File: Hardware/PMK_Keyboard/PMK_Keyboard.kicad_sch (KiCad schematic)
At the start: 51 parts, among them IC1 SN74HC165PWR, IC2 SN74HC165PWR, IC3 SN74HC165PWR, IC4 SN74HC165PWR, IC5 SN74HC165PWR, IC7 ESP32-S2FH4, SW1 SW_Push, SW10 SW_Push, SW11 SW_Push, SW12 SW_Push, SW13 SW_Push, SW14 SW_Push, SW15 SW_Push, SW16 SW_Push, SW17 SW_Push, SW18 SW_Push, SW19 SW_Push, SW2 SW_Push, SW20 SW_Push, SW21 SW_Push, SW22 SW_Push, SW23 SW_Push, SW24 SW_Push, SW25 SW_Push, SW26 SW_Push, SW27 SW_Push, SW28 SW_Push, SW29 SW_Push, SW3 SW_Push, SW30 SW_Push, SW31 SW_Push, SW32 SW_Push, SW33 SW_Push, SW34 SW_Push, SW35 SW_Push, SW36 SW_Push, SW37 SW_Push, SW38 SW_Push, SW39 SW_Push, SW4 SW_Push, SW40 SW_Push, SW5 SW_Push, SW6 SW_Push, SW7 SW_Push, SW8 SW_Push, SW9 SW_Push

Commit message: changed switch footprint
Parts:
- SW1, SW10, SW11, SW12, SW13, SW14, SW15, SW16, SW17, SW18, SW19, SW2, SW20, SW21, SW22, SW23, SW24, SW25, SW26, SW27, SW28, SW29, SW3, SW30, SW31, SW32, SW33, SW34, SW35, SW36, SW37, SW38, SW39, SW4, SW5, SW6, SW7, SW8, SW9: footprint Component_lib:Kailh_socket_PG1350_optional_reversible -> Component_lib:Kailh_socket_PG1350_reversible

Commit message: Started routing
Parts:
- SW40: footprint Component_lib:SKRPABE010 -> Component_lib:Kailh_socket_PG1350_reversible
- SW8: footprint Component_lib:Kailh_socket_PG1350_reversible -> Component_lib:SKRPABE010
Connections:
- net 1: now also SW1.1; no longer SW1.2
- net 10: now also SW10.1; no longer SW10.2
- net 11: now also SW11.1; no longer SW11.2
- net 12: now also SW12.1; no longer SW12.2
- net 13: now also SW13.1; no longer SW13.2
- net 14: now also SW14.1; no longer SW14.2
- net 15: now also SW15.1; no longer SW15.2
- net 16: now also SW16.1; no longer SW16.2
- net 17: now also SW17.1; no longer SW17.2
- net 18: now also SW18.1; no longer SW18.2
- net 19: now also SW19.1; no longer SW19.2
- net 2: now also SW2.1; no longer SW2.2
- net 20: now also SW20.1; no longer SW20.2
- net 21: now also SW21.1; no longer SW21.2
- net 22: now also SW22.1; no longer SW22.2
- net 23: now also SW23.1; no longer SW23.2
- net 24: now also SW24.1; no longer SW24.2
- net 25: now also SW25.1; no longer SW25.2
- net 26: now also SW26.1; no longer SW26.2
- net 27: now also SW27.1; no longer SW27.2
- net 28: now also SW28.1; no longer SW28.2
- net 29: now also SW29.1; no longer SW29.2
- net 3: now also SW3.1; no longer SW3.2
- net 30: now also SW30.1; no longer SW30.2
- net 31: now also SW31.1; no longer SW31.2
- net 32: now also SW32.1; no longer SW32.2
- net 33: now also SW33.1; no longer SW33.2
- net 34: now also SW34.1; no longer SW34.2
- net 35: now also SW35.1; no longer SW35.2
- net 36: now also SW36.1; no longer SW36.2
- net 37: now also SW37.1; no longer SW37.2
- net 38: now also SW38.1; no longer SW38.2
- net 39: now also SW39.1; no longer SW39.2
- net 4: now also SW4.1; no longer SW4.2
- net 40: now also SW40.1; no longer SW40.2
- net 5: now also SW5.1; no longer SW5.2
- net 6: now also SW6.1; no longer SW6.2
- net 7: now also SW7.1; no longer SW7.2
- net 8: now also SW8.1; no longer SW8.2
- net 9: now also SW9.1; no longer SW9.2
- net GND: now also SW1.2, SW10.2, SW11.2, SW12.2, SW13.2, SW14.2, SW15.2, SW16.2, SW17.2, SW18.2, SW19.2, SW2.2, SW20.2, SW21.2, SW22.2, SW23.2, SW24.2, SW25.2, SW26.2, SW27.2, SW28.2, SW29.2, SW3.2, SW30.2, SW31.2, SW32.2, SW33.2, SW34.2, SW35.2, SW36.2, SW37.2, SW38.2, SW39.2, SW4.2, SW40.2, SW5.2, SW6.2, SW7.2, SW8.2, SW9.2; no longer SW1.1, SW10.1, SW11.1, SW12.1, SW13.1, SW14.1, SW15.1, SW16.1, SW17.1, SW18.1, SW19.1, SW2.1, SW20.1, SW21.1, SW22.1, SW23.1, SW24.1, SW25.1, SW26.1, SW27.1, SW28.1, SW29.1, SW3.1, SW30.1, SW31.1, SW32.1, SW33.1, SW34.1, SW35.1, SW36.1, SW37.1, SW38.1, SW39.1, SW4.1, SW40.1, SW5.1, SW6.1, SW7.1, SW8.1, SW9.1
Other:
- moved on the sheet: SW1, SW10, SW11, SW12, SW13, SW14, SW15, SW16, SW17, SW18, SW19, SW2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

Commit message: Added ESP32 to schematic
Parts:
- added ANT?: 2450AT18A100E, ANTC3216X140N, symbol Component lib:2450AT18A100E
- added C? (x3): 10u, symbol Component lib:C
- added C? (x9): 100n, symbol Component lib:C
- added C? (x2): 15p, symbol Component lib:C
- added C? (x2): 1u, symbol Component lib:C
- added C? (x2): C, symbol Component lib:C
- added D?: LED, symbol Component lib:LED
- added J10: USB_C_Receptacle_USB2.0, symbol Connector:USB_C_Receptacle_USB2.0
- added L?: L, symbol Component lib:L
- added R10, R11: 5.1k, symbol Component lib:R
- added R? (x2): 10k, symbol Component lib:R
- added R?: 0, symbol Component lib:R
- added R?: 2k, symbol Component lib:R
- added R?: 0k, symbol Component lib:R
- added S? (x2): SKRPABE010, SKRPABE010, symbol Component lib:SKRPABE010
- added U?: MIC5528-3.3YMT-T5, SON40P120X120X60-7N-D, symbol Component lib:MIC5528-3.3YMT-T5
- added Y?: 40MHz, symbol Device:Crystal_GND23_Small
- IC7: footprint Component_lib:QFN40P700X700X90-57N-D -> QFN40P700X700X90-57N-D
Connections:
- net +3V3: now also IC7.1 (VDDA_1), IC7.20 (VDD3P3_RTC), IC7.27 (VDD3P3_RTC_IO), IC7.3 (VDD3P3_1), IC7.4 (VDD3P3_2), IC7.45 (VDD3P3_CPU), IC7.51 (VDDA_2), IC7.54 (VDDA_3), C?.1, C?.1, C?.1, C?.1, C?.1, C?.1, C?.1, C?.1, C?.1, C?.1, R?.1, R?.1, U?.1 (VOUT_1), U?.2 (VOUT_2)
- net GND: now also IC7.57 (GND), C?.2, C?.2, C?.2, C?.2, C?.2, C?.2, C?.2, C?.2, C?.2, C?.2, C?.2, C?.2, C?.2, C?.2, C?.2, C?.2, C?.2, C?.2, D?.1 (K), J10.A1 (GND), J10.A12 (GND), J10.B1 (GND), J10.B12 (GND), J10.S1 (SHIELD), R10.2, R11.2, S?.2, S?.2, U?.3 (GND), U?.7 (EP), Y?.2, Y?.3
- net IO5: now reaches IC7.10 (GPIO5)
- net IO6: now reaches IC7.11 (GPIO6)
- net IO7: now reaches IC7.12 (GPIO7)
- net IO8: now reaches IC7.13 (GPIO8)
- net IO9: now reaches IC7.14 (GPIO9)
- net IO10: now reaches IC7.15 (GPIO10)
- net IO11: now reaches IC7.16 (GPIO11)
- net IO12: now reaches IC7.17 (GPIO12)
- net IO13: now reaches IC7.18 (GPIO13)
- net IO14: now reaches IC7.19 (GPIO14)
- net LNA_IN: now reaches IC7.2 (LNA_IN)
- net LNA_IN: now also C?.1, L?.2
- net IO15: now reaches IC7.21 (XTAL_32K_P)
- net IO15: now also R?.1
- net IO16: now reaches IC7.22 (XTAL_32K_N)
- net IO17: now reaches IC7.23 (DAC_1)
- net IO18: now reaches IC7.24 (DAC_2)
- net IO18: now also R?.2
- net D-: now reaches IC7.25 (GPIO19)
- net D-: now also J10.A7 (D-), J10.B7 (D-)
- net D+: now reaches IC7.26 (GPIO20)
- net D+: now also J10.A6 (D+), J10.B6 (D+)
- net IO21: now reaches IC7.28 (GPIO21)
- net VDD_SPI: now reaches IC7.30 (VDD_SPI)
- net VDD_SPI: now also C?.1, C?.1
- net IO33: now reaches IC7.37 (GPIO33)
- net IO34: now reaches IC7.38 (GPIO34)
- net IO35: now reaches IC7.39 (GPIO35)
- net IO36: now reaches IC7.40 (GPIO36)
- net IO37: now reaches IC7.41 (GPIO37)
- net IO38: now reaches IC7.42 (GPIO38)
- net IO39: now reaches IC7.43 (MTCK)
- net IO40: now reaches IC7.44 (MTD0)
- net IO41: now reaches IC7.46 (MTDI)
- net IO42: now reaches IC7.47 (MTMS)
- net IO43: now reaches IC7.48 (U0TXD)
- net IO44: now reaches IC7.49 (U0RXD)
- net IO0: now reaches IC7.5 (GPIO0)
- net IO0: now also S?.1
- net IO45: now reaches IC7.50 (GPIO45)
- net at IC7.52 (XTAL_N): now also C?.1, Y?.4
- net at IC7.53 (XTAL_P): now also R?.2
- net IO46: now reaches IC7.55 (GPIO46)
- net EN: now reaches IC7.56 (CHIP_PU)
- net EN: now also C?.1, R?.2, S?.1
- net IO1: now reaches IC7.6 (GPIO1)
- net IO2: now reaches IC7.7 (GPIO2)
- net IO3: now reaches IC7.8 (GPIO3)
- net IO4: now reaches IC7.9 (GPIO4)
- new net: R?.2, U?.4 (EN)
- new net: C?.1, R?.1, Y?.1
- new net: D?.2 (A), R?.2
- new net: ANT?.1 (A), C?.1, L?.1
- new net CC1: J10.A5 (CC1), R11.1
- new net CC2: J10.B5 (CC2), R10.1
- new net VBUS: C?.1, J10.A4 (VBUS), J10.A9 (VBUS), J10.B4 (VBUS), J10.B9 (VBUS), R?.1, U?.6 (VIN)
- no-connect marks 6 -> 15
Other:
- note added: "10-USB"
- note added: "20-Power"
- note added: "30-ESP32"
- note added: "40MHz 10ppm"
- moved on the sheet: IC1, IC2, IC3, IC4, IC5, IC7, RN1, RN2, RN3, RN4, RN5, SW1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

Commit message: Updated schematic
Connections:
- net CLK renamed SPI_CLK
- net MISO renamed SPI_MISO
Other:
- note added: "Boot mode"
- note added: "Reset"
- moved on the sheet: C?, S?

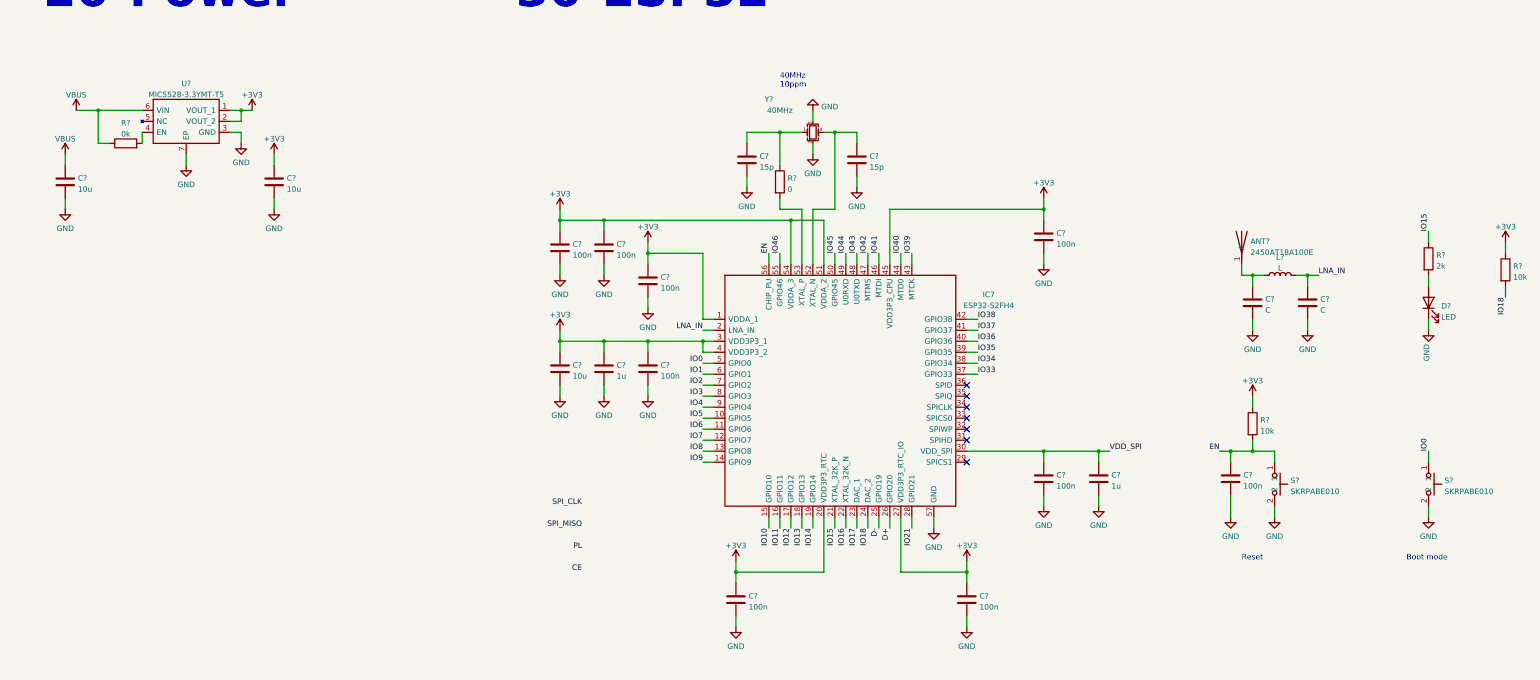
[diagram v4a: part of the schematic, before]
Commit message: Redone routing for 180mm version
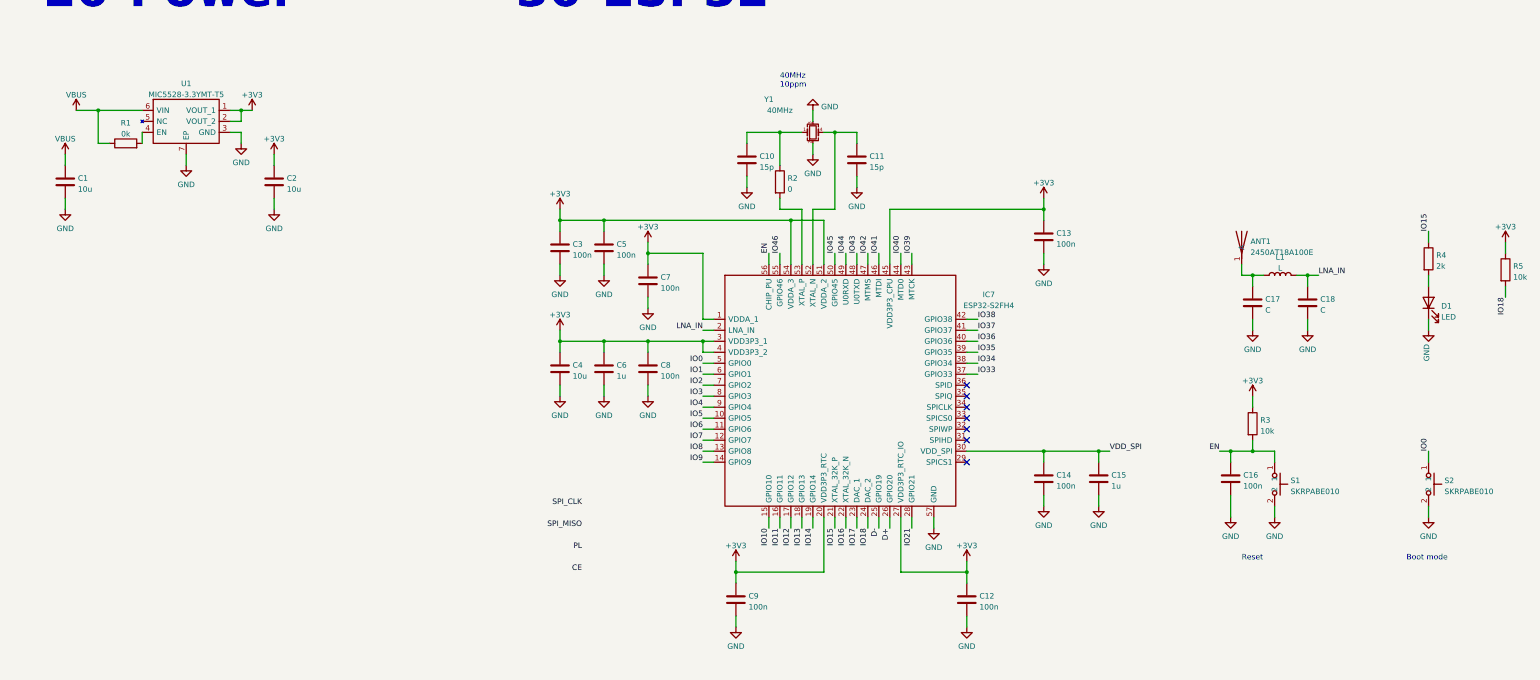
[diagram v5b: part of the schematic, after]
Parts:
- ANT1: renamed from ANT?; footprint ANTC3216X140N -> Component_lib:ANTC3216X140N
- C1, C2, C4: renamed from C?; footprint (none) -> Capacitor_SMD:C_0603_1608Metric
- C10, C11, C17, C18: renamed from C?; footprint (none) -> Capacitor_SMD:C_0201_0603Metric
- C12, C13, C14, C15, C16, C3, C5, C6, C7, C8, C9: renamed from C?; footprint (none) -> Capacitor_SMD:C_0402_1005Metric
- D1: renamed from D?; footprint (none) -> LED_SMD:LED_0402_1005Metric
- IC7: footprint QFN40P700X700X90-57N-D -> Component_lib:QFN40P700X700X90-57N-D
- L1: renamed from L?; footprint (none) -> Inductor_SMD:L_0201_0603Metric
- R1, R2, R3, R4, R5: renamed from R?; footprint (none) -> Resistor_SMD:R_0201_0603Metric
- R10, R11: footprint (none) -> Resistor_SMD:R_0201_0603Metric
- S1, S2: renamed from S?; footprint SKRPABE010 -> Component_lib:SKRPABE010
- SW8: footprint Component_lib:SKRPABE010 -> Component_lib:Kailh_socket_PG1350_reversible
- U1: renamed from U?; footprint SON40P120X120X60-7N-D -> Component_lib:SON40P120X120X60-7N-D
- Y1: renamed from Y?; footprint (none) -> Component_lib:Crystal_SMD_2016-4Pin_2.0x1.6mm

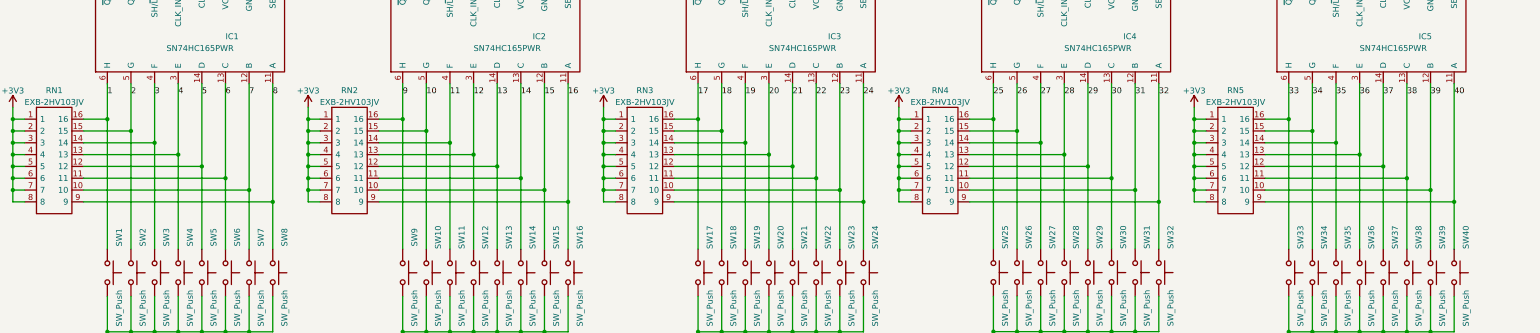
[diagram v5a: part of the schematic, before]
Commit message: Started routing the pullups
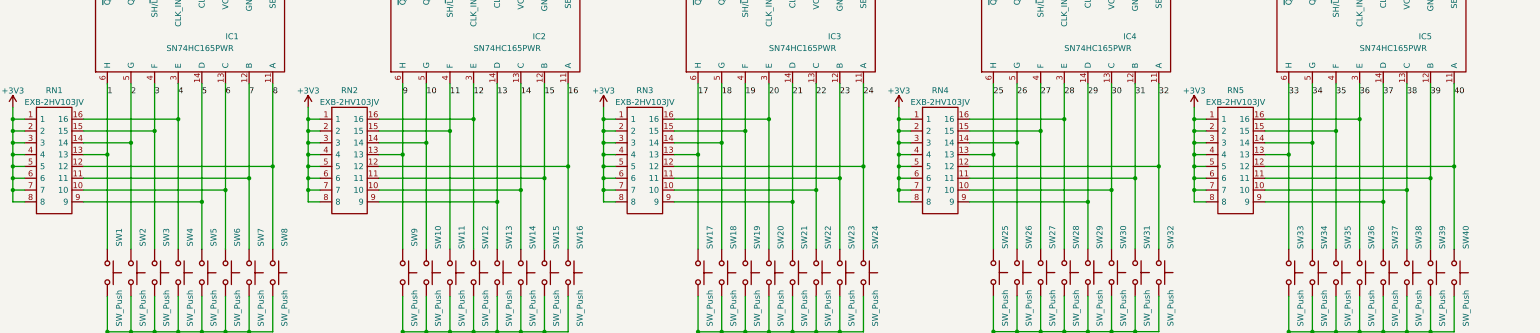
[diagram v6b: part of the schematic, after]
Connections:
- net 1: now also RN1.13; no longer RN1.16
- net 10: now also RN2.14; no longer RN2.15
- net 11: now also RN2.15; no longer RN2.14
- net 12: now also RN2.16; no longer RN2.13
- net 13: now also RN2.9; no longer RN2.12
- net 14: now also RN2.10; no longer RN2.11
- net 15: now also RN2.11; no longer RN2.10
- net 16: now also RN2.12; no longer RN2.9
- net 17: now also RN3.13; no longer RN3.16
- net 18: now also RN3.14; no longer RN3.15
- net 19: now also RN3.15; no longer RN3.14
- net 2: now also RN1.14; no longer RN1.15
- net 20: now also RN3.16; no longer RN3.13
- net 21: now also RN3.9; no longer RN3.12
- net 22: now also RN3.10; no longer RN3.11
- net 23: now also RN3.11; no longer RN3.10
- net 24: now also RN3.12; no longer RN3.9
- net 25: now also RN4.13; no longer RN4.16
- net 26: now also RN4.14; no longer RN4.15
- net 27: now also RN4.15; no longer RN4.14
- net 28: now also RN4.16; no longer RN4.13
- net 29: now also RN4.9; no longer RN4.12
- net 3: now also RN1.15; no longer RN1.14
- net 30: now also RN4.10; no longer RN4.11
- net 31: now also RN4.11; no longer RN4.10
- net 32: now also RN4.12; no longer RN4.9
- net 33: now also RN5.13; no longer RN5.16
- net 34: now also RN5.14; no longer RN5.15
- net 35: now also RN5.15; no longer RN5.14
- net 36: now also RN5.16; no longer RN5.13
- net 37: now also RN5.9; no longer RN5.12
- net 38: now also RN5.10; no longer RN5.11
- net 39: now also RN5.11; no longer RN5.10
- net 4: now also RN1.16; no longer RN1.13
- net 40: now also RN5.12; no longer RN5.9
- net 5: now also RN1.9; no longer RN1.12
- net 6: now also RN1.10; no longer RN1.11
- net 7: now also RN1.11; no longer RN1.10
- net 8: now also RN1.12; no longer RN1.9
- net 9: now also RN2.13; no longer RN2.16

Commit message: Keyboard routing is ongoing
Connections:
- net 33: now also RN5.9; no longer RN5.13
- net 34: now also RN5.10; no longer RN5.14
- net 35: now also RN5.11; no longer RN5.15
- net 36: now also RN5.12; no longer RN5.16
- net 37: now also RN5.13; no longer RN5.9
- net 38: now also RN5.14; no longer RN5.10
- net 39: now also RN5.15; no longer RN5.11
- net 40: now also RN5.16; no longer RN5.12

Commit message: Added LEDs
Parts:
- added C19, C20: 10u, Capacitor_SMD:C_0603_1608Metric, symbol Component lib:C
- added D10, D11, D12, D13, D14, D15, D16, D17, D18, D19, D2, D20, D21, D22, D23, D24, D25, D26, D27, D28, D29, D3, D30, D31, D32, D33, D34, D35, D36, D37, D38, D39, D4, D40, D41, D5, D6, D7, D8, D9: YF923_2020_WS2812_LED, Component_lib:YF923_2020_WS2812_LED_DUALSIDE, symbol Component lib:YF923_2020_WS2812_LED
- added U2: MIC5528-3.3YMT-T5, Component_lib:SON40P120X120X60-7N-D, symbol Component lib:MIC5528-3.3YMT-T5
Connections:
- net IO35 is gone; now on net CE: IC7.39 (GPIO35)
- net PL is gone; now on net IO36: IC1.1 (SH/~{LD}), IC2.1 (SH/~{LD}), IC3.1 (SH/~{LD}), IC4.1 (SH/~{LD}), IC5.1 (SH/~{LD})
- net SPI_CLK is gone; now on net IO38: IC1.2 (CLK), IC2.2 (CLK), IC3.2 (CLK), IC4.2 (CLK), IC5.2 (CLK)
- net SPI_MISO is gone; now on net IO37: IC1.9 (QH)
- net GND: now also C19.2, C20.2, D10.1 (VSS), D11.1 (VSS), D12.1 (VSS), D13.1 (VSS), D14.1 (VSS), D15.1 (VSS), D16.1 (VSS), D17.1 (VSS), D18.1 (VSS), D19.1 (VSS), D2.1 (VSS), D20.1 (VSS), D21.1 (VSS), D22.1 (VSS), D23.1 (VSS), D24.1 (VSS), D25.1 (VSS), D26.1 (VSS), D27.1 (VSS), D28.1 (VSS), D29.1 (VSS), D3.1 (VSS), D30.1 (VSS), D31.1 (VSS), D32.1 (VSS), D33.1 (VSS), D34.1 (VSS), D35.1 (VSS), D36.1 (VSS), D37.1 (VSS), D38.1 (VSS), D39.1 (VSS), D4.1 (VSS), D40.1 (VSS), D41.1 (VSS), D5.1 (VSS), D6.1 (VSS), D7.1 (VSS), D8.1 (VSS), D9.1 (VSS), U2.3 (GND), U2.7 (EP)
- net IO33: now also U2.4 (EN)
- net IO34: now also D2.3 (DIN)
- net VBUS: now also C19.1, U2.6 (VIN)
- new net: D40.4 (DO), D41.3 (DIN)
- new net: D8.4 (DO), D9.3 (DIN)
- new net: D10.3 (DIN), D9.4 (DO)
- new net: D2.4 (DO), D3.3 (DIN)
- new net: D10.4 (DO), D11.3 (DIN)
- new net: D30.4 (DO), D31.3 (DIN)
- new net: D31.4 (DO), D32.3 (DIN)
- new net: D39.4 (DO), D40.3 (DIN)
- new net: D32.4 (DO), D33.3 (DIN)
- new net: D33.4 (DO), D34.3 (DIN)
- new net: D14.4 (DO), D15.3 (DIN)
- new net: D15.4 (DO), D16.3 (DIN)
- new net: D5.4 (DO), D6.3 (DIN)
- new net: D6.4 (DO), D7.3 (DIN)
- new net: D35.4 (DO), D36.3 (DIN)
- new net: D36.4 (DO), D37.3 (DIN)
- new net: D12.4 (DO), D13.3 (DIN)
- new net: D13.4 (DO), D14.3 (DIN)
- new net: D37.4 (DO), D38.3 (DIN)
- new net: D22.4 (DO), D23.3 (DIN)
- new net: D23.4 (DO), D24.3 (DIN)
- new net: D38.4 (DO), D39.3 (DIN)
- new net: D24.4 (DO), D25.3 (DIN)
- new net: D25.4 (DO), D26.3 (DIN)
- new net: D29.4 (DO), D30.3 (DIN)
- new net: D21.4 (DO), D22.3 (DIN)
- new net: D16.4 (DO), D17.3 (DIN)
- new net: D17.4 (DO), D18.3 (DIN)
- new net: D3.4 (DO), D4.3 (DIN)
- new net: D4.4 (DO), D5.3 (DIN)
- new net: D28.4 (DO), D29.3 (DIN)
- new net: D11.4 (DO), D12.3 (DIN)
- new net: D26.4 (DO), D27.3 (DIN)
- new net: D27.4 (DO), D28.3 (DIN)
- new net: D20.4 (DO), D21.3 (DIN)
- new net: D18.4 (DO), D19.3 (DIN)
- new net: D34.4 (DO), D35.3 (DIN)
- new net: D19.4 (DO), D20.3 (DIN)
- new net: D7.4 (DO), D8.3 (DIN)
- new net VDD: C20.1, D10.2 (VDD), D11.2 (VDD), D12.2 (VDD), D13.2 (VDD), D14.2 (VDD), D15.2 (VDD), D16.2 (VDD), D17.2 (VDD), D18.2 (VDD), D19.2 (VDD), D2.2 (VDD), D20.2 (VDD), D21.2 (VDD), D22.2 (VDD), D23.2 (VDD), D24.2 (VDD), D25.2 (VDD), D26.2 (VDD), D27.2 (VDD), D28.2 (VDD), D29.2 (VDD), D3.2 (VDD), D30.2 (VDD), D31.2 (VDD), D32.2 (VDD), D33.2 (VDD), D34.2 (VDD), D35.2 (VDD), D36.2 (VDD), D37.2 (VDD), D38.2 (VDD), D39.2 (VDD), D4.2 (VDD), D40.2 (VDD), D41.2 (VDD), D5.2 (VDD), D6.2 (VDD), D7.2 (VDD), D8.2 (VDD), D9.2 (VDD), U2.1 (VOUT_1), U2.2 (VOUT_2)
